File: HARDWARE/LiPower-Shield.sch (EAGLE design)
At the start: 52 parts, among them U1 MAX17043G+U, U2 TPS61200, U3 MCP73831, U4 ARDUINO_R3_SHIELD, X1 USBSMD

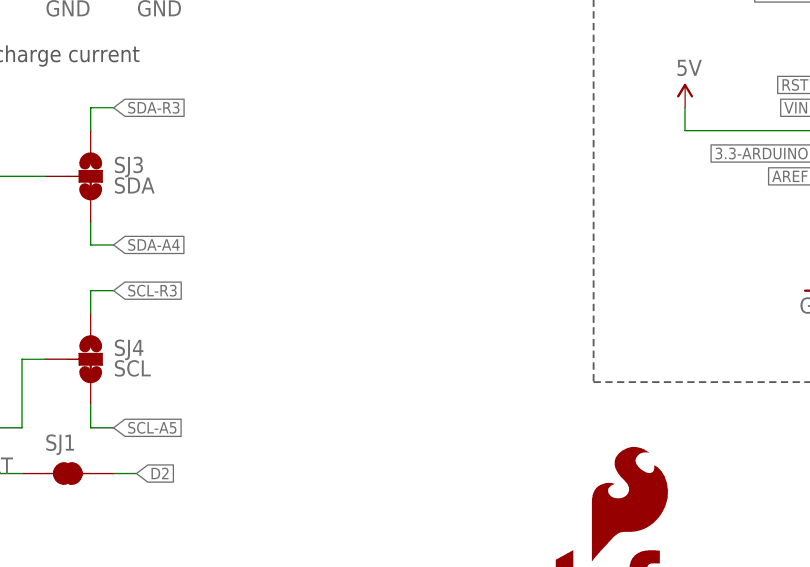
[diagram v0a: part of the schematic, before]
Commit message: Added info on SDA/SCL jumpers
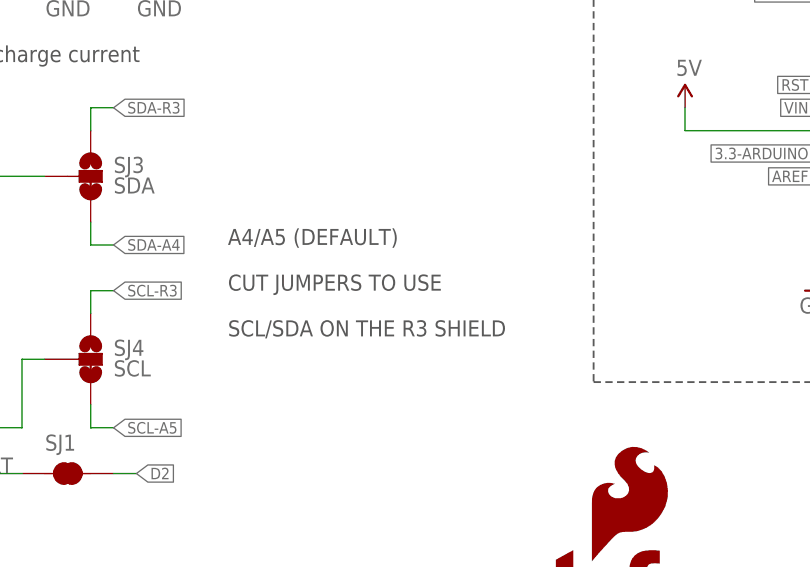
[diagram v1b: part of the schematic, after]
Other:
- note added: "A4/A5 (DEFAULT)"
- note added: "CUT JUMPERS TO USE"
- note added: "SCL/SDA ON THE R3 SHIELD"
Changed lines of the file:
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@@
 <wire x1="106.68" y1="35.56" x2="147.32" y2="35.56" width="0.2032" layer="97" style="shortdash"/>
 <wire x1="147.32" y1="35.56" x2="147.32" y2="33.02" width="0.2032" layer="97" style="shortdash"/>
+<text x="142.24" y="83.82" size="1.778" layer="97">A4/A5 (DEFAULT)</text>
+<text x="142.24" y="78.74" size="1.778" layer="97">CUT JUMPERS TO USE</text>
+<text x="142.24" y="73.66" size="1.778" layer="97">SCL/SDA ON THE R3 SHIELD</text>
 </plain>
 <instances>

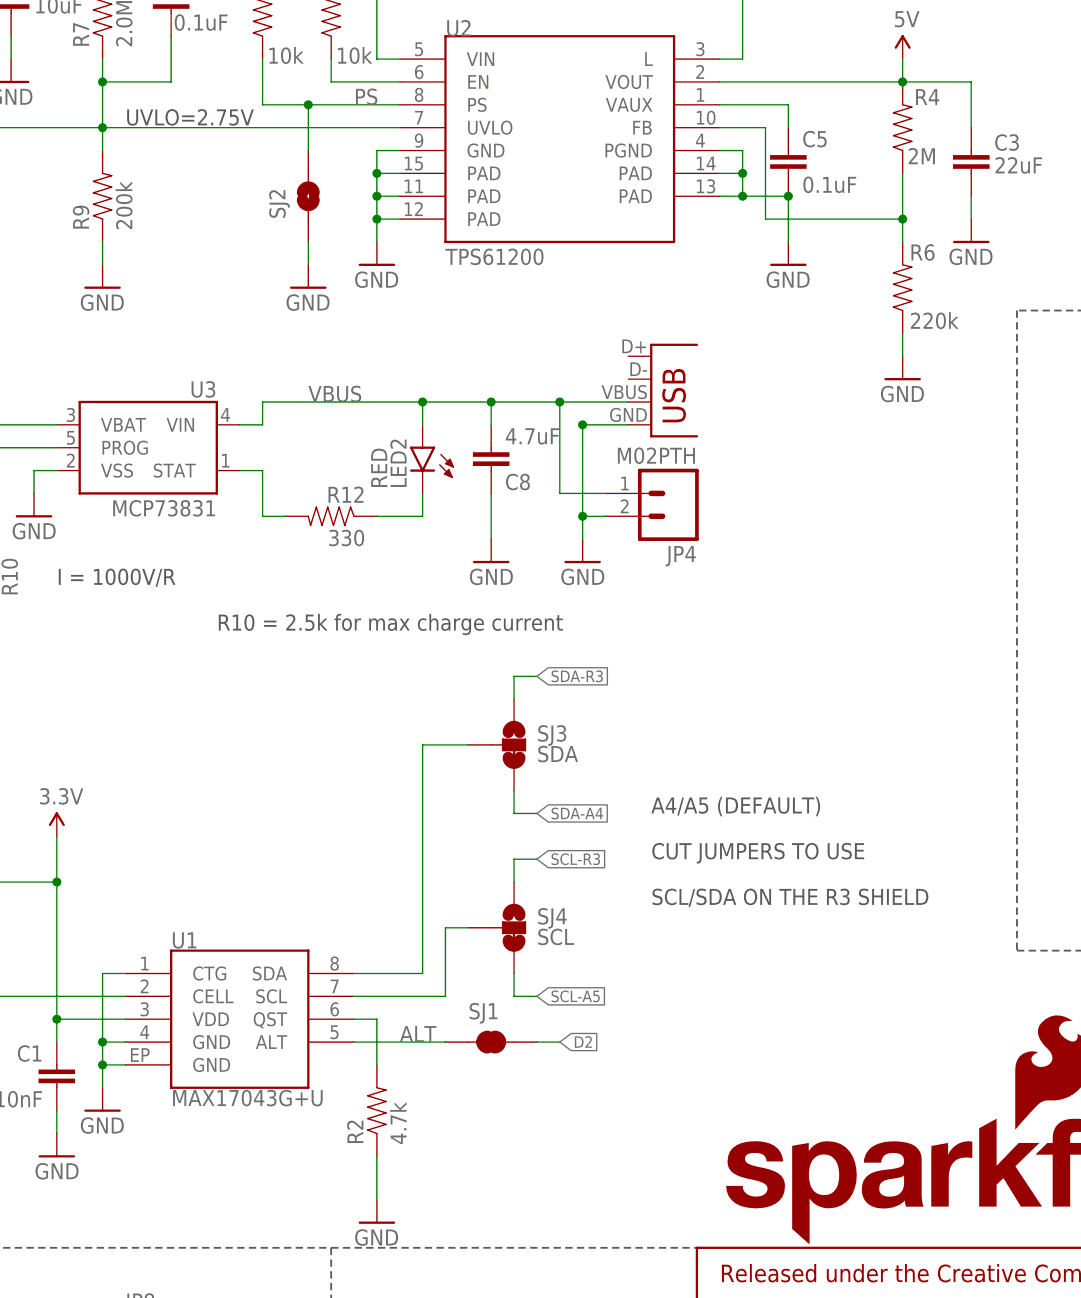
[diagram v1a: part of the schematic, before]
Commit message: Adding descriptions to SJ1 and SJ2.
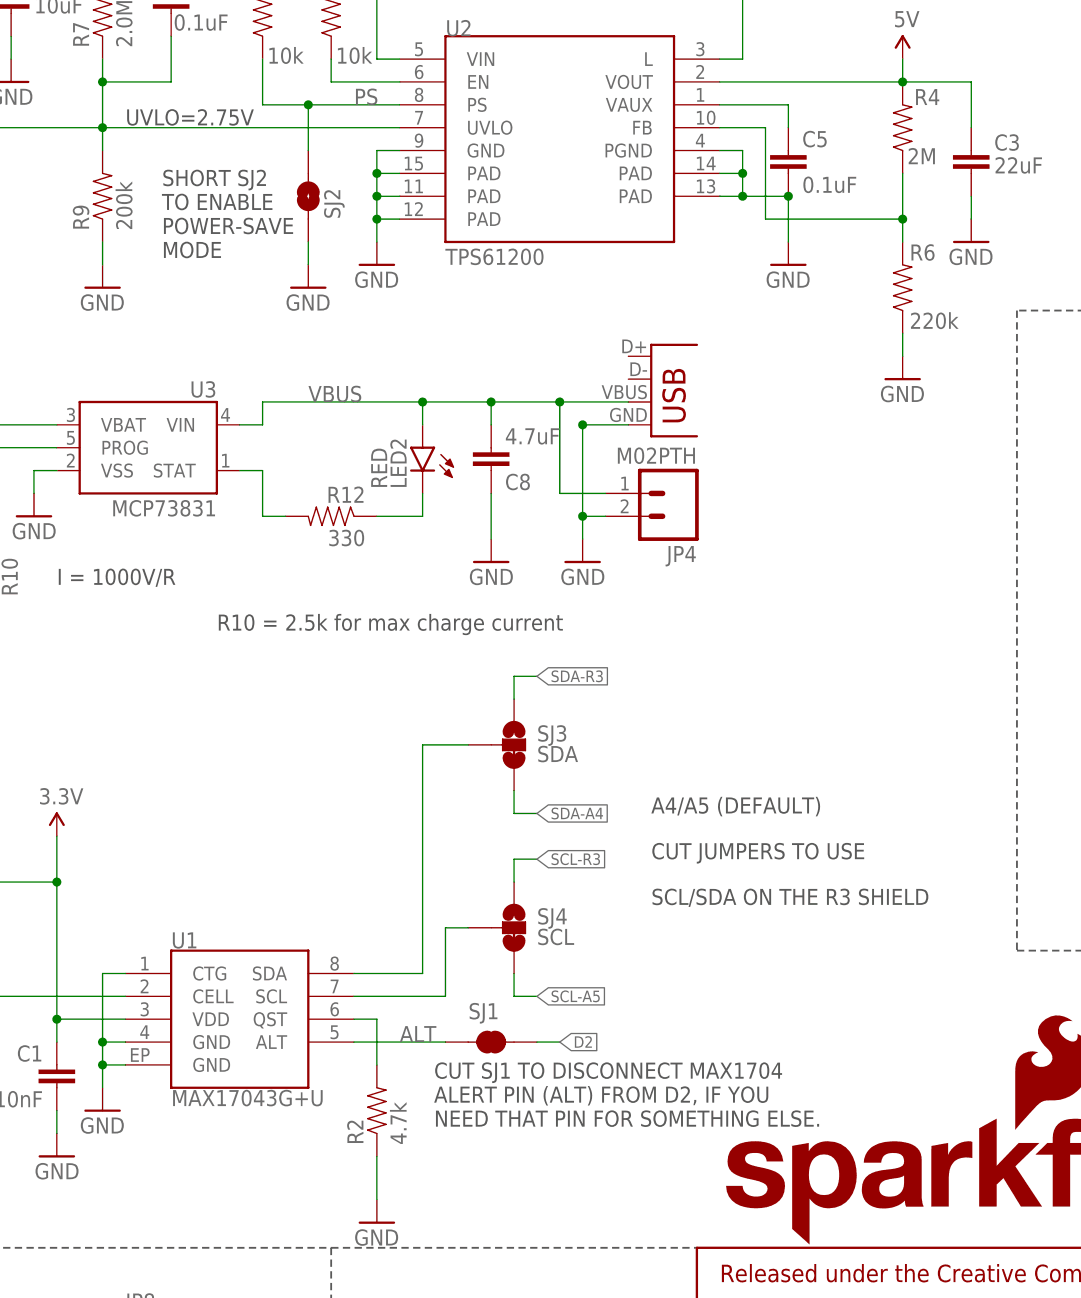
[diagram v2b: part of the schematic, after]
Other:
- note added: "CUT SJ1 TO DISCONNECT MAX1704 ALERT PIN (ALT) FROM D2, IF YOU NEED THAT PIN FOR SOMETHING ELSE."
- note added: "SHORT SJ2 TO ENABLE POWER-SAVE MODE"
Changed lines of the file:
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@@
 <?xml version="1.0" encoding="utf-8"?>
 <!DOCTYPE eagle SYSTEM "eagle.dtd">
-<eagle version="6.4">
+<eagle version="7.1.0">
 <drawing>
 <settings>
@@
 <text x="142.24" y="78.74" size="1.778" layer="97">CUT JUMPERS TO USE</text>
 <text x="142.24" y="73.66" size="1.778" layer="97">SCL/SDA ON THE R3 SHIELD</text>
+<text x="87.884" y="145.542" size="1.778" layer="97">SHORT SJ2
+TO ENABLE
+POWER-SAVE
+MODE</text>
+<text x="118.11" y="49.022" size="1.778" layer="97">CUT SJ1 TO DISCONNECT MAX1704
+ALERT PIN (ALT) FROM D2, IF YOU
+NEED THAT PIN FOR SOMETHING ELSE.</text>
 </plain>
 <instances>
@@
 <instance part="U$4" gate="G$1" x="170.18" y="167.64"/>
 <instance part="SJ2" gate="1" x="104.14" y="152.4" smashed="yes" rot="R90">
-<attribute name="NAME" x="101.6" y="149.86" size="1.778" layer="95" rot="R90"/>
+<attribute name="NAME" x="107.696" y="149.86" size="1.778" layer="95" rot="R90"/>
 </instance>
 <instance part="GND17" gate="1" x="104.14" y="142.24"/>
@@
 </schematic>
 </drawing>
+<compatibility>
+<note version="6.3" minversion="6.2.2" severity="warning">
+Since Version 6.2.2 text objects can contain more than one line,
+which will not be processed correctly with this version.
+</note>
+</compatibility>
 </eagle>

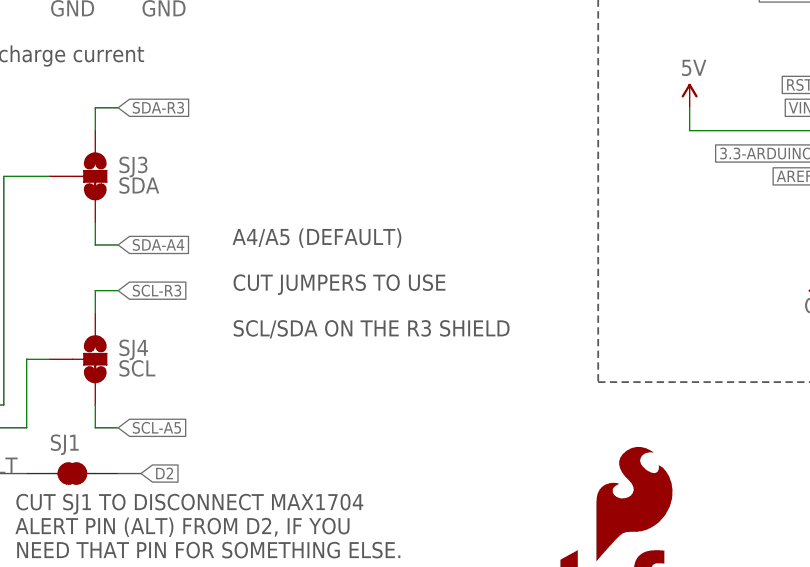
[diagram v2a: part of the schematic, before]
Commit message: Reduced paste on IC's
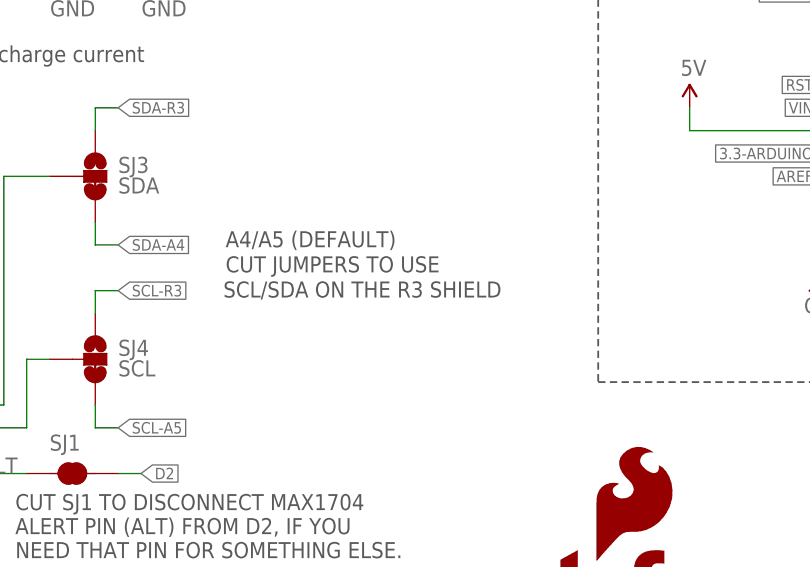
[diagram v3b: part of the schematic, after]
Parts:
- U1: device SparkFun:MAX1704X -> SparkFun-PowerIC:MAX1704X
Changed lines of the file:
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@@
 <?xml version="1.0" encoding="utf-8"?>
 <!DOCTYPE eagle SYSTEM "eagle.dtd">
-<eagle version="7.1.0">
+<eagle version="6.4">
 <drawing>
 <settings>
@@
 <part name="FRAME1" library="SparkFun-Aesthetics" deviceset="FRAME-LETTER" device=""/>
 <part name="U4" library="SparkFun-Boards" deviceset="ARDUINO_R3_SHIELD" device=""/>
-<part name="U1" library="SparkFun" deviceset="MAX1704X" device="" value="MAX17043G+U"/>
+<part name="U1" library="SparkFun-PowerIC" deviceset="MAX1704X" device="" value="MAX17043G+U"/>
 <part name="C1" library="SparkFun-Capacitors" deviceset="10NF/10000PF-50V-10%(0603)" device="" value="10nF"/>
 <part name="GND3" library="SparkFun" deviceset="GND" device=""/>
@@
 <wire x1="106.68" y1="35.56" x2="147.32" y2="35.56" width="0.2032" layer="97" style="shortdash"/>
 <wire x1="147.32" y1="35.56" x2="147.32" y2="33.02" width="0.2032" layer="97" style="shortdash"/>
-<text x="142.24" y="83.82" size="1.778" layer="97">A4/A5 (DEFAULT)</text>
-<text x="142.24" y="78.74" size="1.778" layer="97">CUT JUMPERS TO USE</text>
-<text x="142.24" y="73.66" size="1.778" layer="97">SCL/SDA ON THE R3 SHIELD</text>
+<text x="141.478" y="83.566" size="1.778" layer="97">A4/A5 (DEFAULT)</text>
+<text x="141.478" y="80.772" size="1.778" layer="97">CUT JUMPERS TO USE</text>
+<text x="141.224" y="77.978" size="1.778" layer="97">SCL/SDA ON THE R3 SHIELD</text>
 <text x="87.884" y="145.542" size="1.778" layer="97">SHORT SJ2
 TO ENABLE

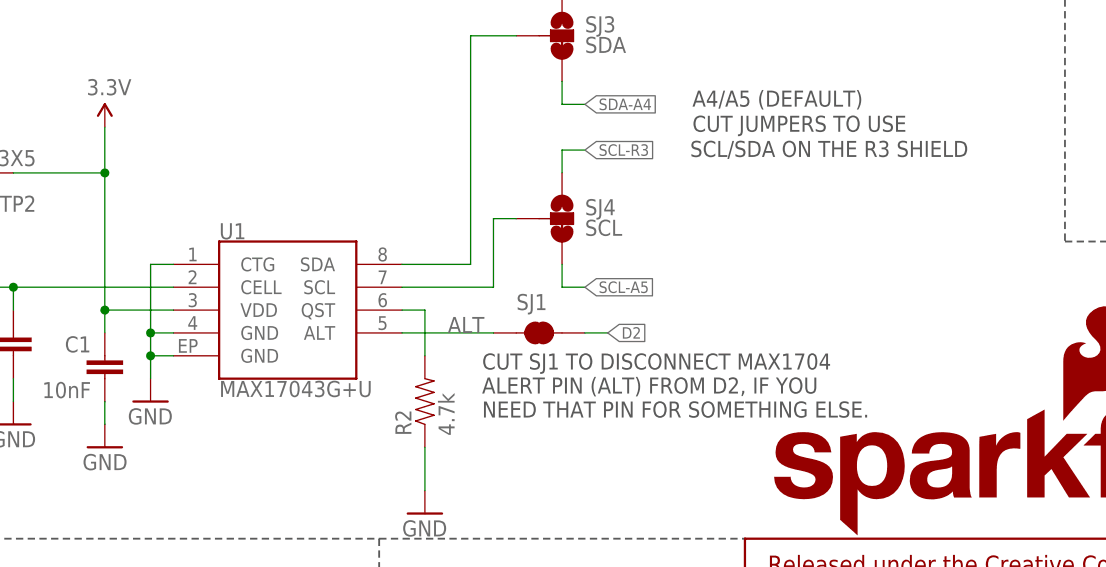
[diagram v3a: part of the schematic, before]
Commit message: Adding MAX17043G I2C address to schematic.
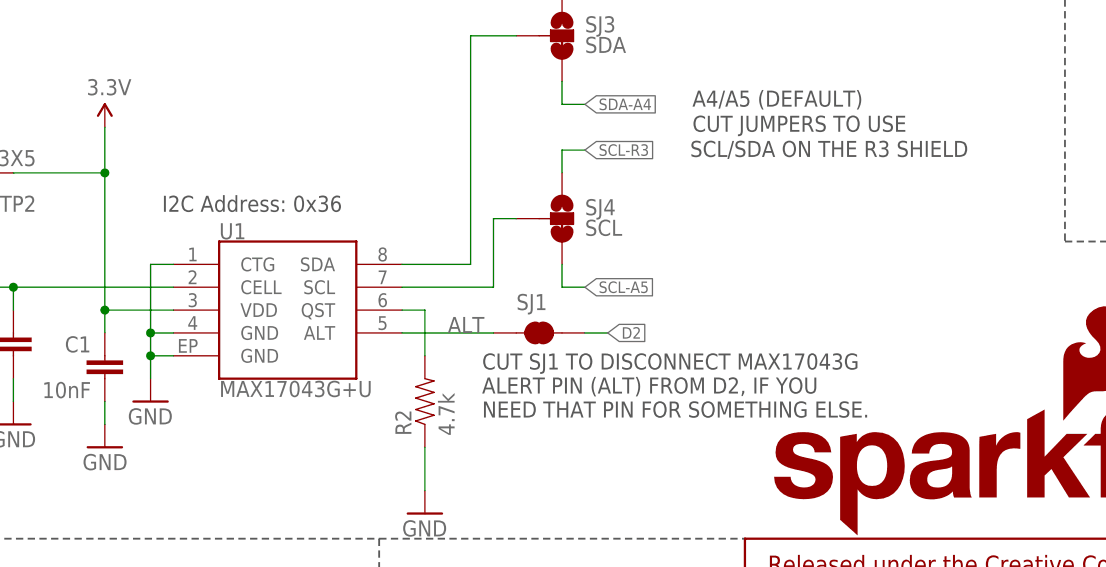
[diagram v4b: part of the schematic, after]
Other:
- note added: "CUT SJ1 TO DISCONNECT MAX17043G ALERT PIN (ALT) FROM D2, IF YOU NEED THAT PIN FOR SOMETHING ELSE."
- note added: "I2C Address: 0x36"
- note removed: "CUT SJ1 TO DISCONNECT MAX1704 ALERT PIN (ALT) FROM D2, IF YOU NEED THAT PIN FOR SOMETHING ELSE."
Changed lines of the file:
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@@
 <?xml version="1.0" encoding="utf-8"?>
 <!DOCTYPE eagle SYSTEM "eagle.dtd">
-<eagle version="6.4">
+<eagle version="7.1.0">
 <drawing>
 <settings>
@@
 POWER-SAVE
 MODE</text>
-<text x="118.11" y="49.022" size="1.778" layer="97">CUT SJ1 TO DISCONNECT MAX1704
+<text x="118.11" y="49.022" size="1.778" layer="97">CUT SJ1 TO DISCONNECT MAX17043G
 ALERT PIN (ALT) FROM D2, IF YOU
 NEED THAT PIN FOR SOMETHING ELSE.</text>
+<text x="82.55" y="71.882" size="1.778" layer="97">I2C Address: 0x36</text>
 </plain>
 <instances>

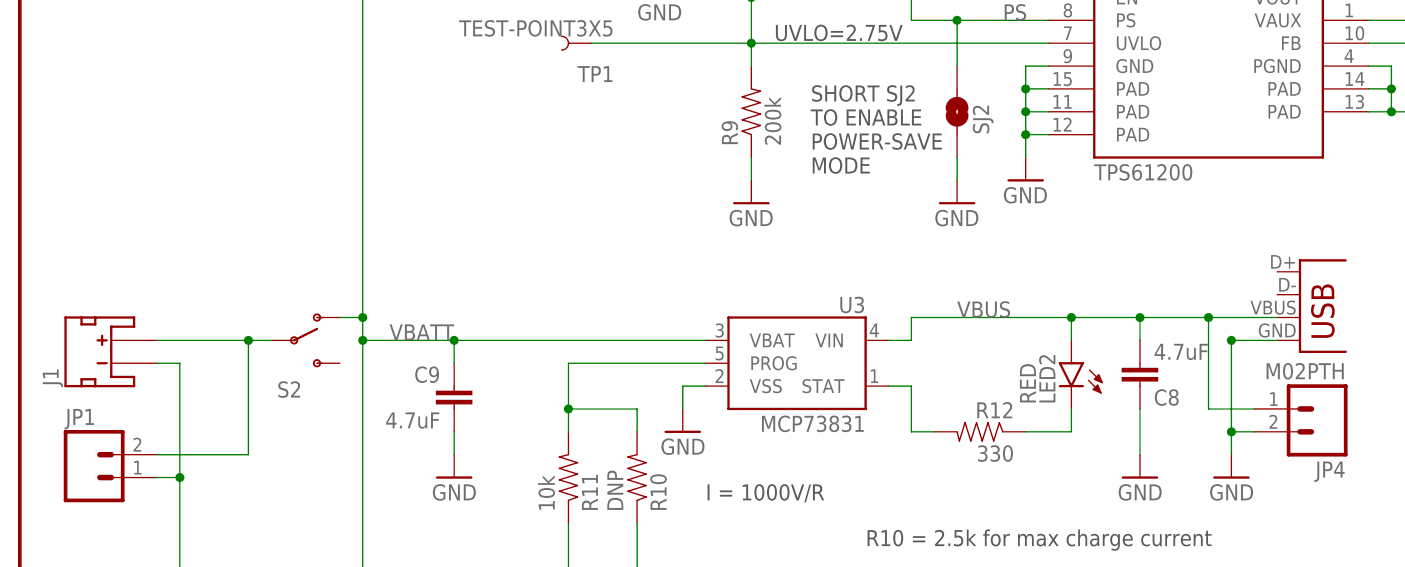
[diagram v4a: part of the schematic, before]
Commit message: Adding voltage input range notes.
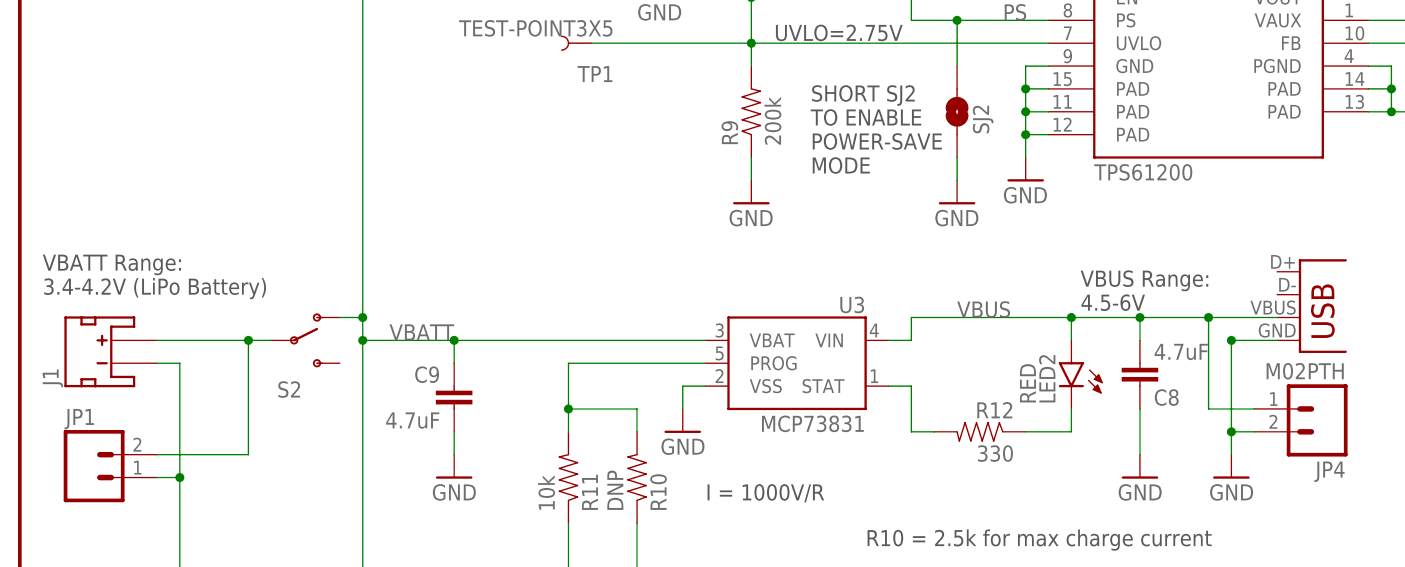
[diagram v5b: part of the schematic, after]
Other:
- note added: "VBATT Range: 3.4-4.2V (LiPo Battery)"
- note added: "VBUS Range: 4.5-6V"
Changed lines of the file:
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@@
 NEED THAT PIN FOR SOMETHING ELSE.</text>
 <text x="82.55" y="71.882" size="1.778" layer="97">I2C Address: 0x36</text>
+<text x="2.54" y="132.08" size="1.778" layer="97">VBATT Range:
+3.4-4.2V (LiPo Battery)
+</text>
+<text x="117.856" y="130.302" size="1.778" layer="97">VBUS Range:
+4.5-6V
+</text>
 </plain>
 <instances>

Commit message: Added prod id's for nduc/caps
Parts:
- C3: device CH_passive:CAP0805 -> SparkFun-Capacitors:22UF-6.3V-20%(0805)
- C4: device CH_passive:CAP1206 -> SparkFun-Capacitors:10UF-6.3V-20%(1206)
- L1: device SparkFun:INDUCTOR. -> SparkFun-Passives:INDUCTORINDUCTOR_4.7UH
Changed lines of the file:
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@@
 <?xml version="1.0" encoding="utf-8"?>
 <!DOCTYPE eagle SYSTEM "eagle.dtd">
-<eagle version="7.1.0">
+<eagle version="6.4">
 <drawing>
 <settings>
@@
 <part name="U$5" library="SparkFun" deviceset="5V" device=""/>
 <part name="GND14" library="SparkFun" deviceset="GND" device=""/>
-<part name="C3" library="CH_passive" deviceset="CAP" device="0805" value="22uF"/>
+<part name="C3" library="SparkFun-Capacitors" deviceset="22UF-6.3V-20%(0805)" device="" value="22uF"/>
 <part name="U2" library="SparkFun-PowerIC" deviceset="TPS61200" device=""/>
 <part name="C6" library="SparkFun-Capacitors" deviceset="0.1UF-25V(+80/-20%)(0603)" device="" value="0.1uF"/>
@@
 <part name="GND4" library="SparkFun" deviceset="GND" device=""/>
 <part name="R4" library="SparkFun-Resistors" deviceset="2MOHMS-1/10W-1%(0603)" device="" value="2M"/>
-<part name="C4" library="CH_passive" deviceset="CAP" device="1206" value="10uF"/>
+<part name="C4" library="SparkFun-Capacitors" deviceset="10UF-6.3V-20%(1206)" device="" value="10uF"/>
 <part name="GND5" library="SparkFun" deviceset="GND" device=""/>
 <part name="GND6" library="SparkFun" deviceset="GND" device=""/>
 <part name="GND16" library="SparkFun" deviceset="GND" device=""/>
-<part name="L1" library="SparkFun" deviceset="INDUCTOR" device="." value="4.7uH, 1.2A"/>
+<part name="L1" library="SparkFun-Passives" deviceset="INDUCTOR" device="INDUCTOR_4.7UH" value="4.7uH, 1.2A"/>
 <part name="GND18" library="SparkFun" deviceset="GND" device=""/>
 <part name="GND21" library="SparkFun" deviceset="GND" device=""/>
